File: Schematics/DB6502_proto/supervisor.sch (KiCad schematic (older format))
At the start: 21 parts

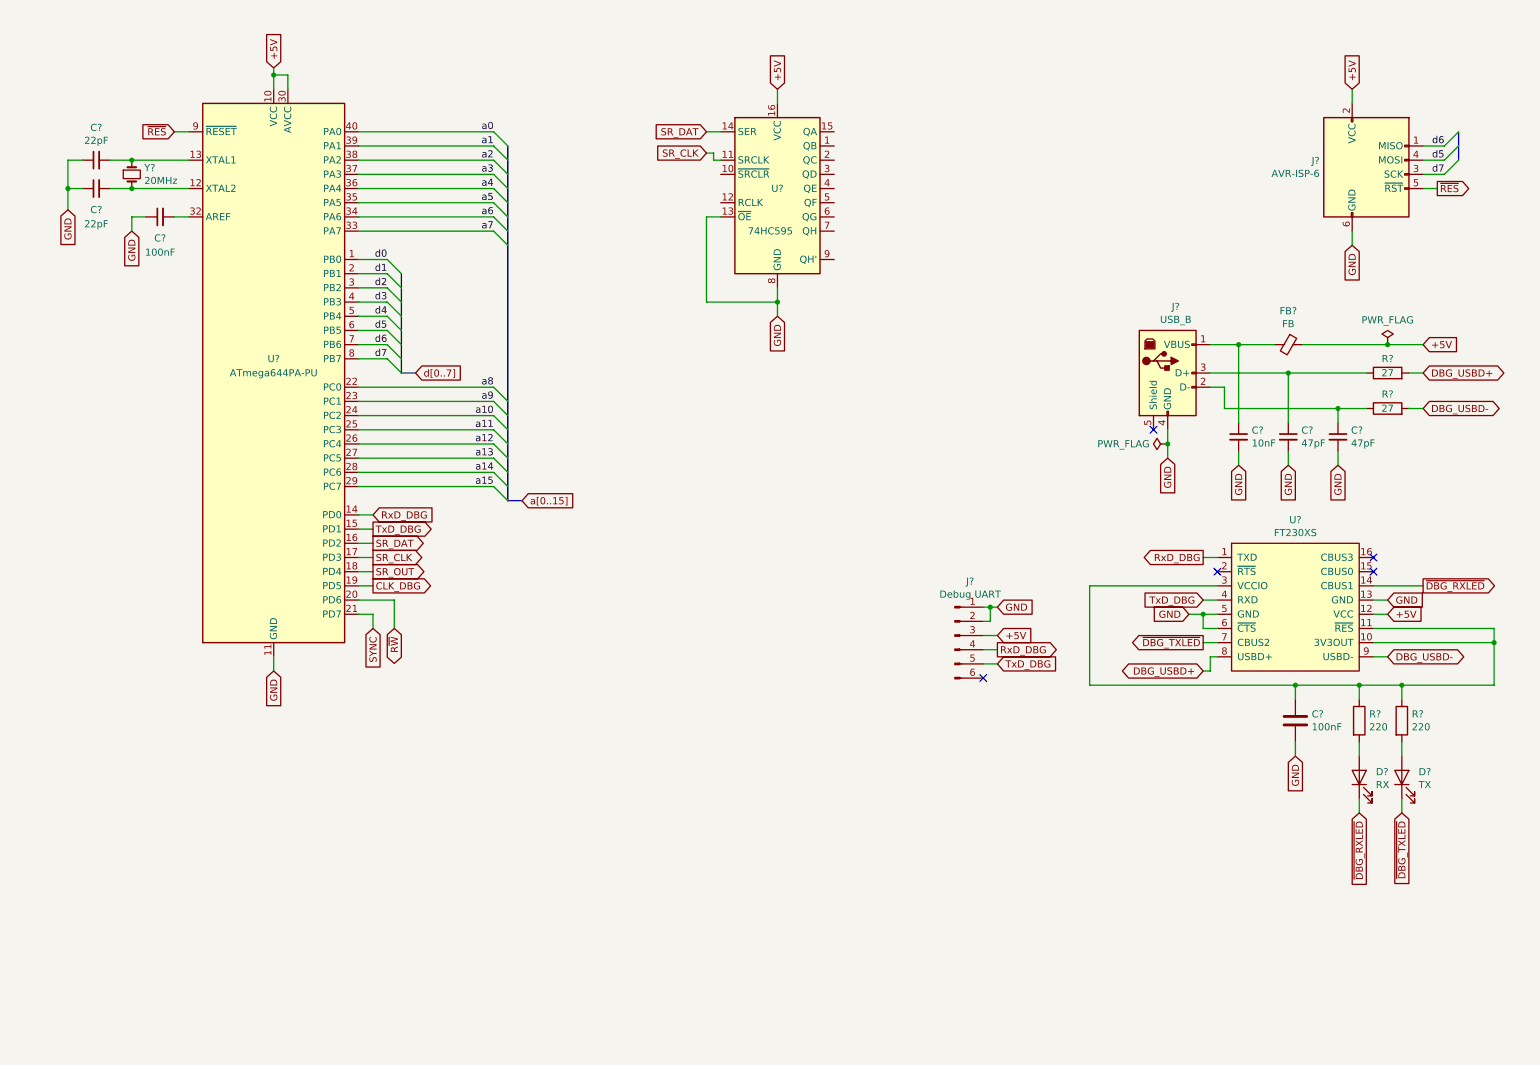
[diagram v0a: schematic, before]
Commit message: Updated supervisor schematic
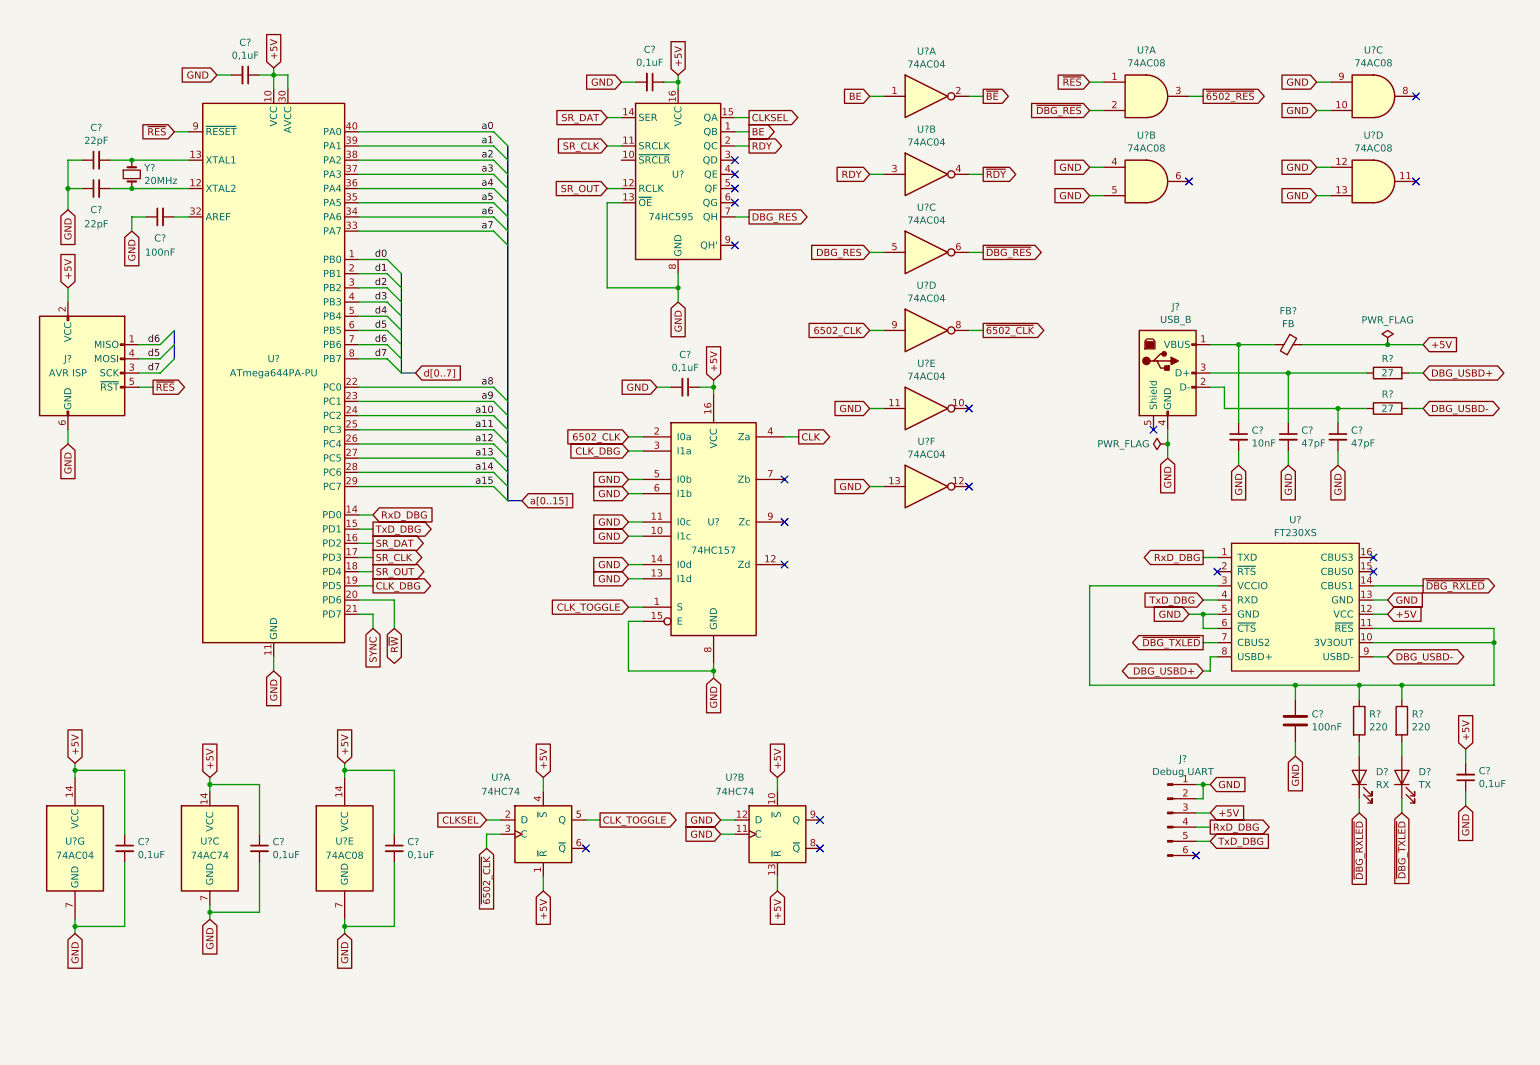
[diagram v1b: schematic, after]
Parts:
- added C? (x7): 0,1uF, symbol Device:C_Small
- added U? (x7): 74AC04, symbol 74xx:74LS04
- added U? (x5): 74AC08, symbol 74xx:74LS08
- added U?: 74HC157, symbol 74xx:74LS157
- added U?: 74AC74, symbol 74xx:74HC74
- added U? (x2): 74HC74, symbol 74xx:74HC74
- J?: value AVR-ISP-6 -> AVR ISP
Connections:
- net +5V: now also C?.1, C?.1, C?.1, C?.1, C?.1, C?.1, C?.2, U?.1 (~R), U?.10 (~S), U?.13 (~R), U?.14 (VCC), U?.14 (VCC), U?.14 (VCC), U?.16 (VCC), U?.4 (~S)
- net CLK_DBG: now also U?.3 (I1a)
- net GND: now also C?.1, C?.2, C?.2, C?.2, C?.2, C?.2, C?.2, U?.10, U?.10 (I1c), U?.11, U?.11 (C), U?.11 (I0c), U?.12, U?.12 (D), U?.13, U?.13, U?.13 (I1d), U?.14 (I0d), U?.15 (E), U?.4, U?.5, U?.5 (I0b), U?.6 (I1b), U?.7 (GND), U?.7 (GND), U?.7 (GND), U?.8 (GND), U?.9
- net SR_OUT: now also U?.12 (RCLK)
- net ~RES: now also U?.1
- net BE: now reaches U?.1 (QB)
- net BE: now also U?.1
- net CLKSEL: now reaches U?.15 (QA)
- net CLKSEL: now also U?.2 (D)
- net RDY: now reaches U?.2 (QC)
- net RDY: now also U?.3
- net DBG_RES: now reaches U?.7 (QH)
- net DBG_RES: now also U?.5
- new net 6502_CLK: U?.2 (I0a), U?.9
- new net CLK: U?.4 (Za)
- new net CLK_TOGGLE: U?.1 (S), U?.5 (Q)
- new net ~6502_CLK: U?.3 (C), U?.8
- new net ~6502_RES: U?.3
- new net ~BE: U?.2
- new net ~DBG_RES: U?.2, U?.6
- new net ~RDY: U?.4
- no-connect marks 5 -> 21
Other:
- moved on the sheet: J?, U?

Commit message: Implemented wait state generator, cleaned up schematic
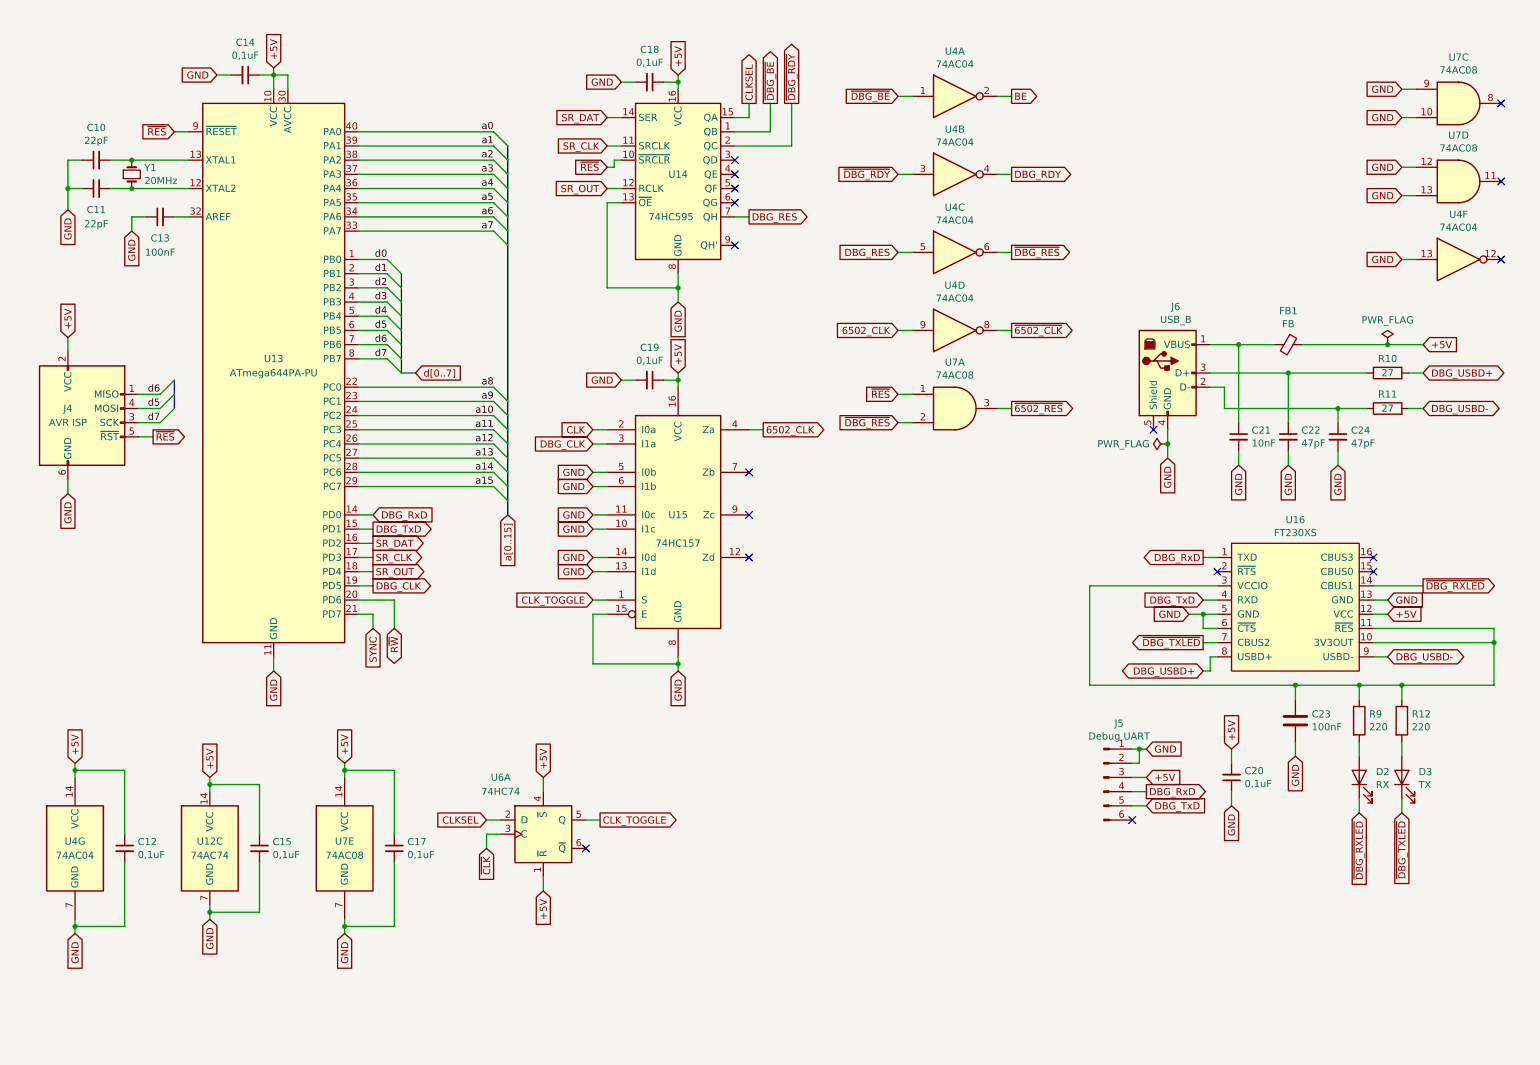
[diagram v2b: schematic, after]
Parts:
- removed U?: 74AC04, symbol 74xx:74LS04
- removed U?: 74HC74, symbol 74xx:74HC74
- removed U?: 74AC08, symbol 74xx:74LS08
- gave numbers to parts that had none: 33
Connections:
- net ~BE is gone; now on net BE: U4.2
- net 6502_CLK: now also U15.4 (Za); no longer U15.2 (I0a)
- net BE: no longer U14.1 (QB), U4.1
- net CLK: now also U15.2 (I0a); no longer U15.4 (Za)
- net ~6502_CLK: no longer U6.3 (C)
- net ~RES: now also U14.10 (~SRCLR)
- net CLK_DBG renamed DBG_CLK
- net RDY renamed ~DBG_RDY
- net RxD_DBG renamed DBG_RxD
- net TxD_DBG renamed DBG_TxD
- net ~RDY renamed DBG_RDY
- new net ~CLK: U6.3 (C)
- new net ~DBG_BE: U14.1 (QB), U4.1
- no-connect marks 21 -> 17
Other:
- moved on the sheet: C19, C20, J4, J5, U15, U4A, U4B, U4C, U4D, U4F, U7A, U7C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

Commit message: Added I/O schematics page with DUART chip
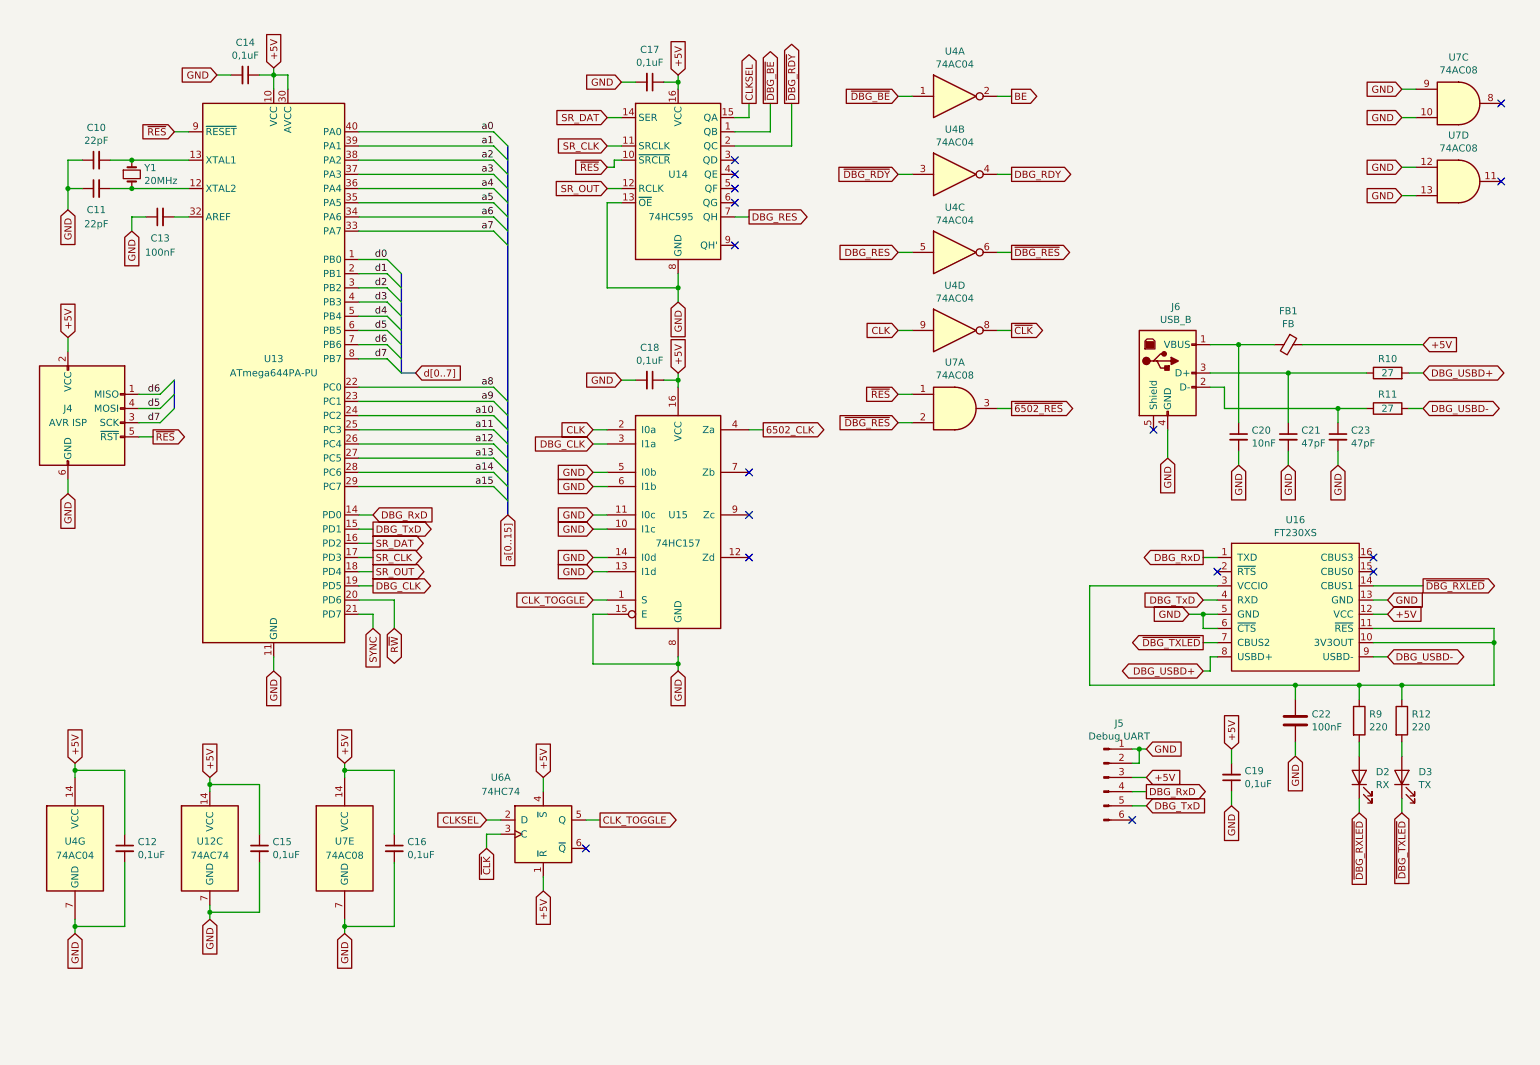
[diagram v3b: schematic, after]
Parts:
- removed unit 6 of U4
- renumbered C17 to C16, C18 to C17, C19 to C18, C20 to C19, C21 to C20, C22 to C21, C23 to C22, C24 to C23
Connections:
- net ~6502_CLK is gone; now on net ~CLK: U4.8
- net 6502_CLK: no longer U4.9
- net CLK: now also U4.9
- no-connect marks 17 -> 16
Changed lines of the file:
@@
 $Descr A4 11693 8268
 encoding utf-8
-Sheet 3 3
+Sheet 3 4
 Title "DB6502 Hobby Computer Version 2"
 Date "2020-10-13"
@@
 Text GLabel 8600 3500 3    50   Input ~ 0
 GND
-Wire Wire Line
-	8600 3400 8600 3300
 $Comp
 L Device:Ferrite_Bead_Small FB?
@@
 	8900 2700 9100 2700
 Wire Wire Line
-	9550 2700 10150 2700
-Wire Wire Line
 	8900 3000 9000 3000
 $Comp
@@
 P 9500 5350
 AR Path="/6014B4D9/5F9AD1F3" Ref="C?"  Part="1"
-AR Path="/5F8F4E1E/5F9AD1F3" Ref="C23"  Part="1"
-F 0 "C23" H 9615 5396 50  0000 L CNN
+AR Path="/5F8F4E1E/5F9AD1F3" Ref="C22"  Part="1"
+F 0 "C22" H 9615 5396 50  0000 L CNN
 F 1 "100nF" H 9615 5305 50  0000 L CNN
 F 2 "Capacitor_THT:C_Disc_D5.0mm_W2.5mm_P2.50mm" H 9538 5200 50  0001 C CNN
@@
 P 9450 3350
 AR Path="/6014B4D9/5F9AD23C" Ref="C?"  Part="1"
-AR Path="/5F8F4E1E/5F9AD23C" Ref="C22"  Part="1"
-F 0 "C22" H 9542 3396 50  0000 L CNN
+AR Path="/5F8F4E1E/5F9AD23C" Ref="C21"  Part="1"
+F 0 "C21" H 9542 3396 50  0000 L CNN
 F 1 "47pF" H 9542 3305 50  0000 L CNN
 F 2 "Capacitor_THT:C_Disc_D5.0mm_W2.5mm_P2.50mm" H 9450 3350 50  0001 C CNN
@@
 P 9800 3350
 AR Path="/6014B4D9/5F9AD242" Ref="C?"  Part="1"
-AR Path="/5F8F4E1E/5F9AD242" Ref="C24"  Part="1"
-F 0 "C24" H 9892 3396 50  0000 L CNN
+AR Path="/5F8F4E1E/5F9AD242" Ref="C23"  Part="1"
+F 0 "C23" H 9892 3396 50  0000 L CNN
 F 1 "47pF" H 9892 3305 50  0000 L CNN
 F 2 "Capacitor_THT:C_Disc_D5.0mm_W2.5mm_P2.50mm" H 9800 3350 50  0001 C CNN
@@
 P 9100 3350
 AR Path="/6014B4D9/5F9AD254" Ref="C?"  Part="1"
-AR Path="/5F8F4E1E/5F9AD254" Ref="C21"  Part="1"
-F 0 "C21" H 9192 3396 50  0000 L CNN
+AR Path="/5F8F4E1E/5F9AD254" Ref="C20"  Part="1"
+F 0 "C20" H 9192 3396 50  0000 L CNN
 F 1 "10nF" H 9192 3305 50  0000 L CNN
 F 2 "Capacitor_THT:C_Disc_D5.0mm_W2.5mm_P2.50mm" H 9100 3350 50  0001 C CNN
@@
 Wire Wire Line
 	9100 3550 9100 3450
-$Comp
-L power:PWR_FLAG #FLG?
-U 1 1 5F9AD25F
-P 10150 2700
-AR Path="/6014B4D9/5F9AD25F" Ref="#FLG?"  Part="1"
-AR Path="/5F8F4E1E/5F9AD25F" Ref="#FLG02"  Part="1"
-F 0 "#FLG02" H 10150 2775 50  0001 C CNN
-F 1 "PWR_FLAG" H 10150 2873 50  0000 C CNN
-F 2 "" H 10150 2700 50  0001 C CNN
-F 3 "~" H 10150 2700 50  0001 C CNN
-	1    10150 2700
-	1    0    0    -1
-$EndComp
-Connection ~ 10150 2700
-Wire Wire Line
-	10150 2700 10400 2700
 $Comp
 L Connector:Conn_01x06_Male J?
@@
 	8450 5950 8350 5950
 $Comp
-L power:PWR_FLAG #FLG?
-U 1 1 5F9AD27A
-P 8600 3400
-AR Path="/6014B4D9/5F9AD27A" Ref="#FLG?"  Part="1"
-AR Path="/5F8F4E1E/5F9AD27A" Ref="#FLG01"  Part="1"
-F 0 "#FLG01" H 8600 3475 50  0001 C CNN
-F 1 "PWR_FLAG" V 8600 3527 50  0000 L CNN
-F 2 "" H 8600 3400 50  0001 C CNN
-F 3 "~" H 8600 3400 50  0001 C CNN
-	1    8600 3400
-	0    -1   -1   0
-$EndComp
-Wire Wire Line
-	8600 3500 8600 3400
-Connection ~ 8600 3400
-$Comp
 L 74xx:74HC595 U14
 U 1 1 5F9C2188
@@
 	1    0    0    -1
 $EndComp
-$Comp
-L 74xx:74LS04 U4
-U 6 1 5F95C43F
-P 10650 2100
-F 0 "U4" H 10650 2417 50  0000 C CNN
-F 1 "74AC04" H 10650 2326 50  0000 C CNN
-F 2 "" H 10650 2100 50  0001 C CNN
-F 3 "https://www.ti.com/lit/ds/symlink/sn74ac04.pdf" H 10650 2100 50  0001 C CNN
-	6    10650 2100
-	1    0    0    -1
-$EndComp
 Text GLabel 6700 2050 0    50   Input ~ 0
 DBG_RES
@@
 Wire Wire Line
 	6700 2600 6800 2600
-Text GLabel 10250 2100 0    50   Input ~ 0
-GND
-Wire Wire Line
-	10250 2100 10350 2100
-NoConn ~ 10950 2100
 Text GLabel 7500 2050 2    50   Output ~ 0
 ~DBG_RES
@@
 	5150 4950 5150 4900
 Text GLabel 6700 2600 0    50   Input ~ 0
-6502_CLK
+CLK
 Text GLabel 7500 2600 2    50   Output ~ 0
-~6502_CLK
+~CLK
 Wire Wire Line
 	7400 2600 7500 2600
@@
 	1850 5800 1850 5850
 $Comp
-L Device:C_Small C19
+L Device:C_Small C18
 U 1 1 5FAF8D14
 P 4950 2950
-F 0 "C19" V 4721 2950 50  0000 C CNN
+F 0 "C18" V 4721 2950 50  0000 C CNN
 F 1 "0,1uF" V 4812 2950 50  0000 C CNN
 F 2 "" H 4950 2950 50  0001 C CNN
@@
 GND
 $Comp
-L Device:C_Small C17
+L Device:C_Small C16
 U 1 1 5FB0F869
 P 3150 6250
-F 0 "C17" H 3242 6296 50  0000 L CNN
+F 0 "C16" H 3242 6296 50  0000 L CNN
 F 1 "0,1uF" H 3242 6205 50  0000 L CNN
 F 2 "" H 3150 6250 50  0001 C CNN
@@
 	2200 800  2300 800
 $Comp
-L Device:C_Small C18
+L Device:C_Small C17
 U 1 1 5FB5019A
 P 4950 850
-F 0 "C18" V 4721 850 50  0000 C CNN
+F 0 "C17" V 4721 850 50  0000 C CNN
 F 1 "0,1uF" V 4812 850 50  0000 C CNN
 F 2 "" H 4950 850 50  0001 C CNN
@@
 NoConn ~ 10950 1000
 $Comp
-L Device:C_Small C20
+L Device:C_Small C19
 U 1 1 5FC939BD
 P 9050 5750
-F 0 "C20" H 8958 5704 50  0000 R CNN
+F 0 "C19" H 8958 5704 50  0000 R CNN
 F 1 "0,1uF" H 8958 5795 50  0000 R CNN
 F 2 "" H 9050 5750 50  0001 C CNN
@@
 Wire Wire Line
 	4700 1400 4750 1400
+Wire Wire Line
+	8600 3300 8600 3500
+Wire Wire Line
+	9550 2700 10400 2700
 Wire Bus Line
 	1600 2950 1600 3150
